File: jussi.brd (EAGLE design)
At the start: 88.9 x 50.8 mm, 35 parts

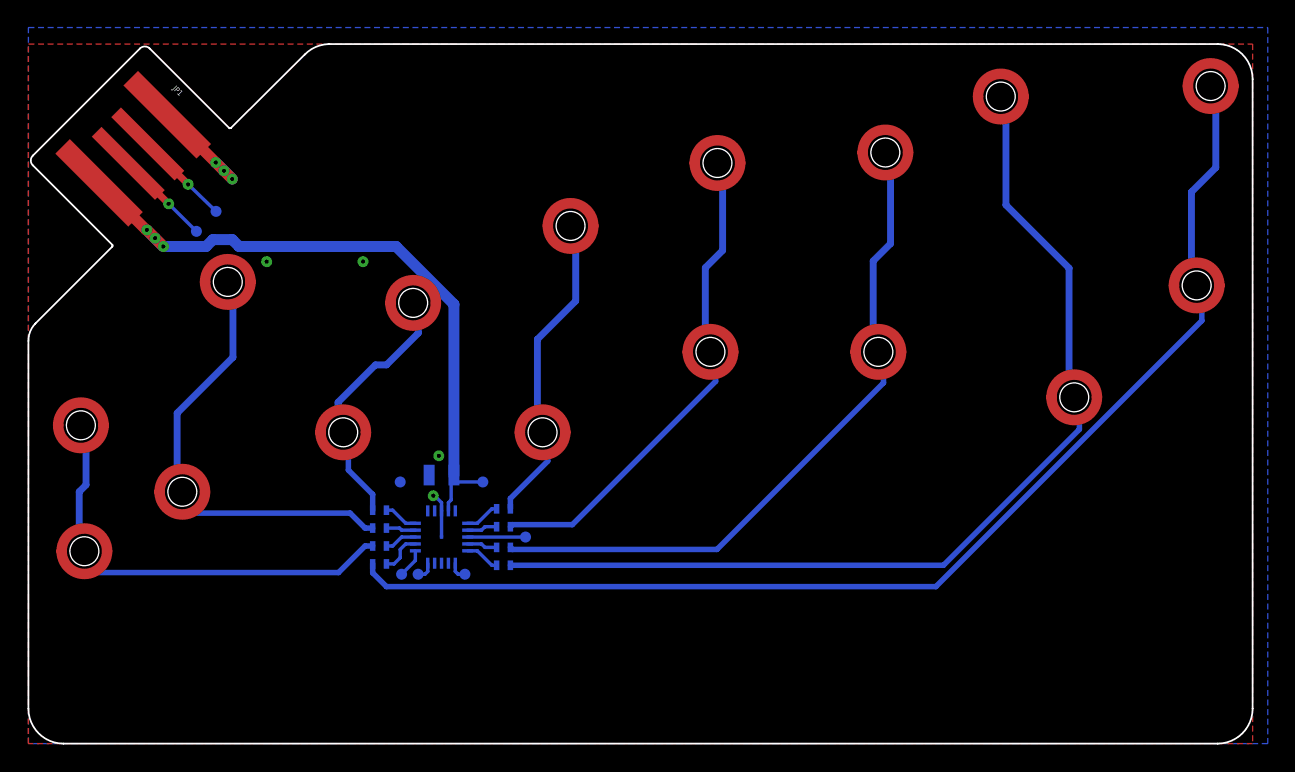
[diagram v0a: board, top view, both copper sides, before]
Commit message: Moving LEDs
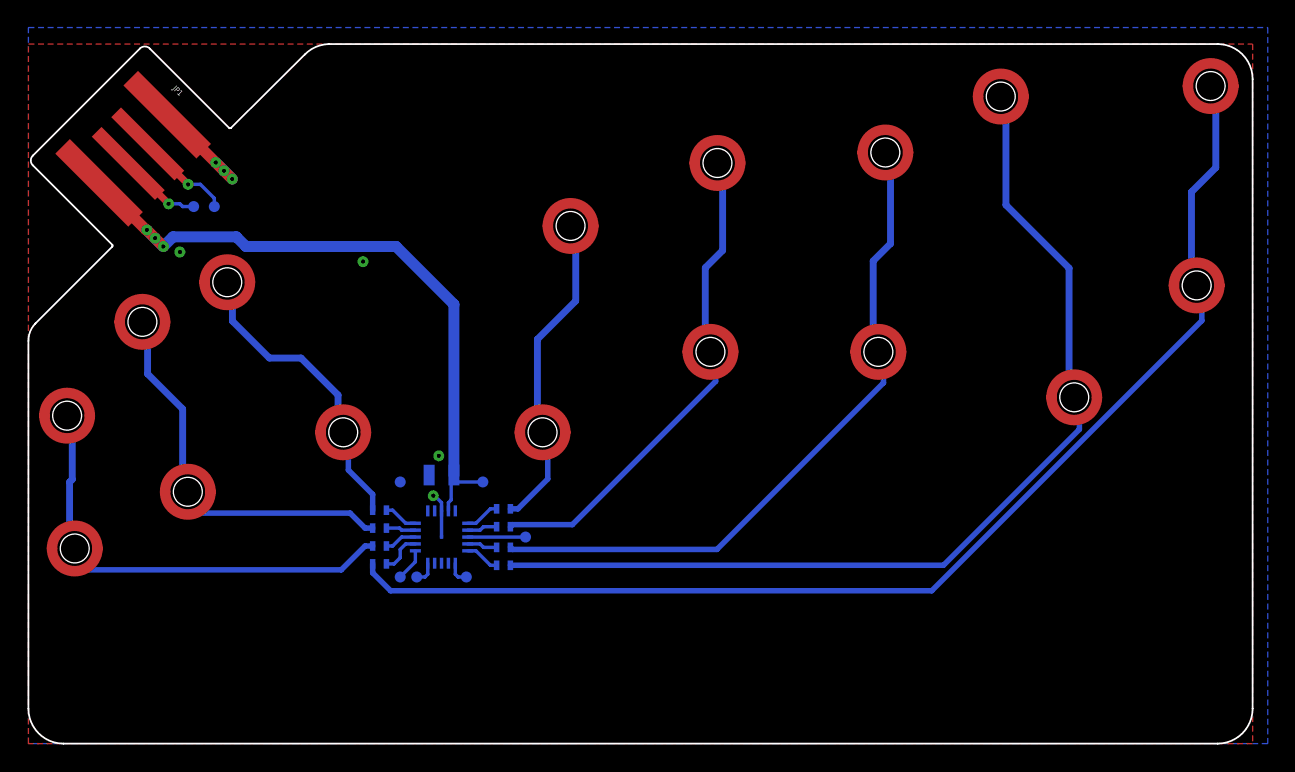
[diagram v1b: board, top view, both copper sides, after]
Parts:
- moved D6 13.6 mm to (14.4, 33.5)
- moved D4 6.84 mm to (8.28, 30.6)
- moved D- 1.81 mm to (12.0, 39.0)
- moved D2 1.22 mm to (2.81, 23.8)
- moved D1 0.73 mm to (3.36, 14.2)
- moved D3 0.40 mm to (11.6, 18.3)
- moved D+ 0.37 mm to (13.5, 39.0)
- moved MISO 0.22 mm to (28.2, 12.1)
- moved MOSI 0.22 mm to (31.8, 12.1)
- moved SCK 0.22 mm to (27.0, 12.1)
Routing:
- net N$2: track 13.8 -> 10.3 mm
- net N$3: track 9.18 -> 12.3 mm
- net D-: track 6.99 -> 6.05 mm
- net N$9: track 21.4 -> 22.0 mm
